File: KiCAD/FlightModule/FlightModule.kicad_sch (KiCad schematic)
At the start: 22 parts, among them Q1 AO3400A, Q2 AO3400A, U1 ARDUINO_MKR_WAN_1310, U2 MCP2515-xST, U3 MCP2562-E-SN, U4 MB85RQ8MX, U5 MB85RQ8MX, U6 MB85RQ8MX, U7 74AHC1G14, U8 L7805

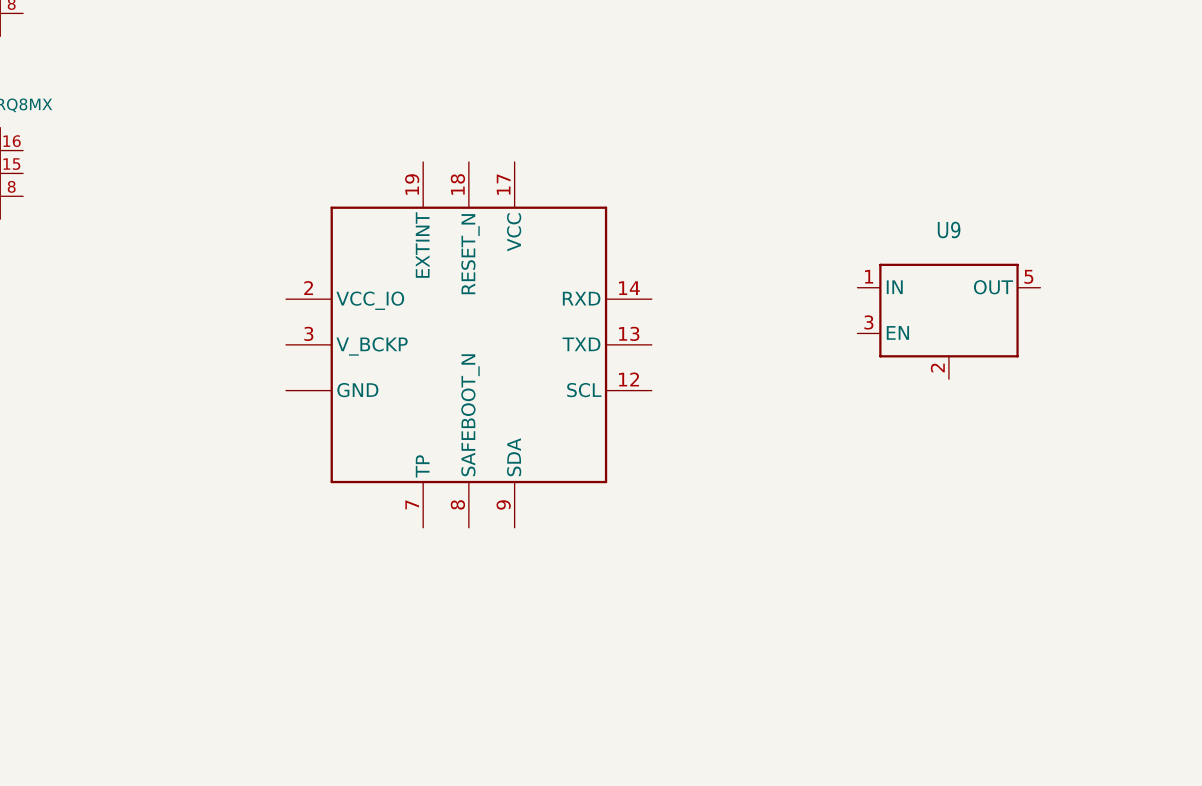
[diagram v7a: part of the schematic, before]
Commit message: ap2112k周りの配線を記載
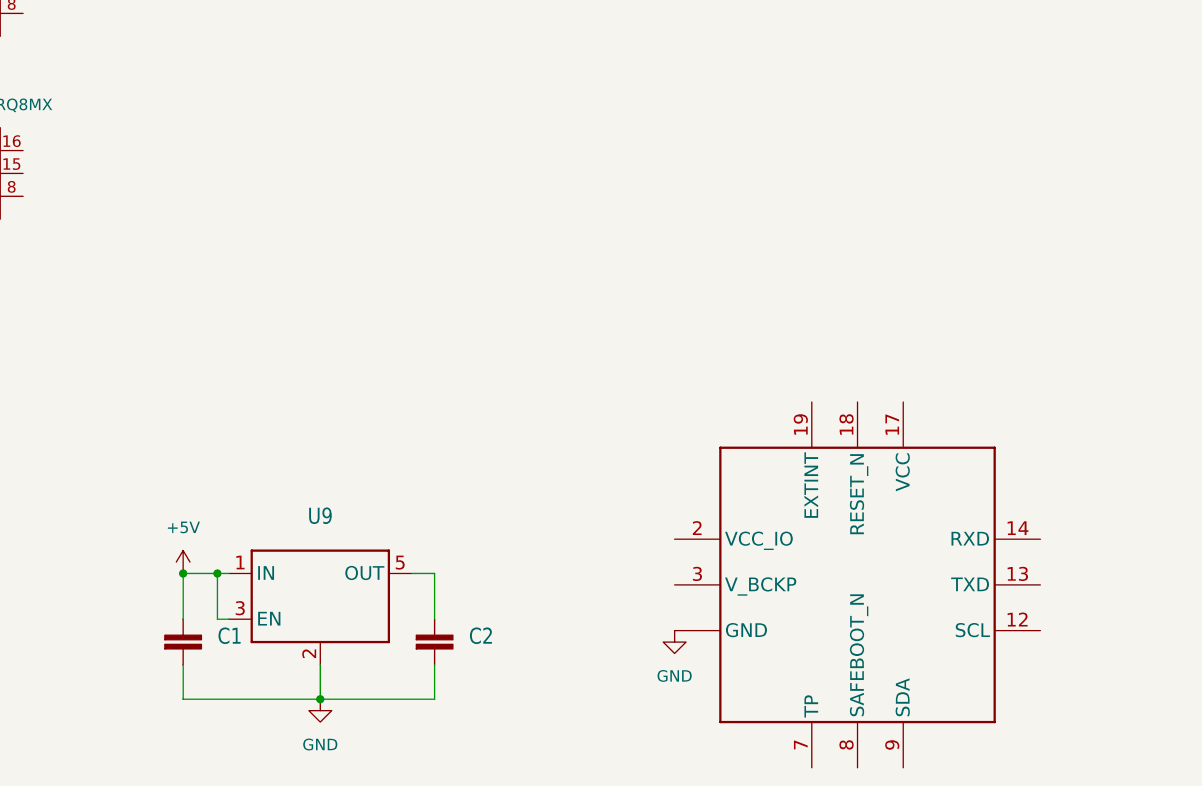
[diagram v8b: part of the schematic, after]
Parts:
- added C1, C2: ~, MKRGPSShield_V4.0:0402-1005X55N, symbol MKRGPSShield_V4.0-eagle-import:Arduino-rcl_C-0402
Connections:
- net GND: now also IC1.1 (GND), IC1.10 (GND), IC1.11 (GND), IC1.15 (GND), IC1.16 (GND), IC1.20 (GND), IC1.4 (GND), IC1.5 (GND), IC1.6 (GND), U9.2 (GND/ADJ), C1.2, C2.2
- net +5V: now reaches U9.1 (IN)
- net +5V: now also U9.3 (EN), C1.1
- net at U9.5 (OUT): now also C2.1
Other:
- moved on the sheet: U9
